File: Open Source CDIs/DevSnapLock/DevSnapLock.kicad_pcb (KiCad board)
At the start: 2 copper layers, 65.5 x 31.5 mm, 19 parts, among them J1 MAG, J2 COIL, J3 GtD, J4 AtG, J5 scrD, J6 lD, J7 aD, J8 aC, Q1 TIC106

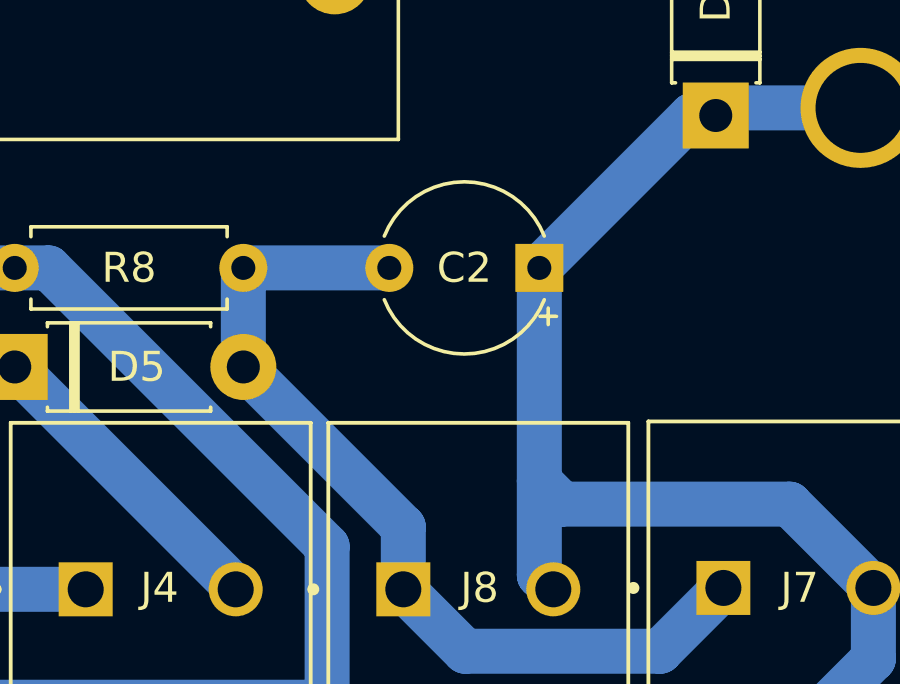
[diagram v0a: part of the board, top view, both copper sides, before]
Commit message: Added new CDIs and updated README
Added the DevPot_v2 CDI, updated the readme to include all of the new CDIs and included images for each. Also add production exports for all the boards.
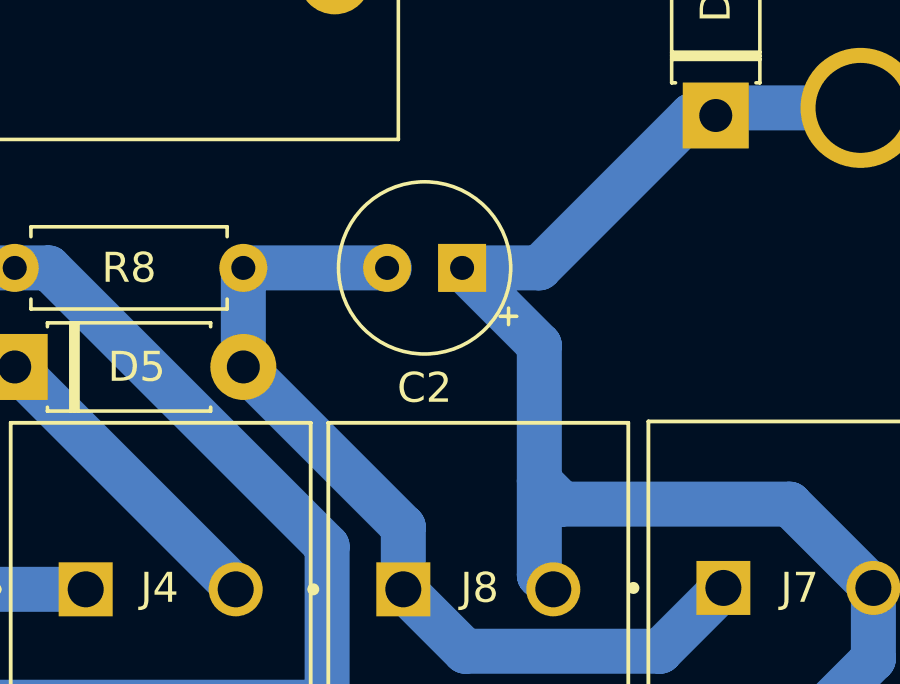
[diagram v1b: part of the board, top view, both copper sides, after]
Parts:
- C2: footprint Capacitor_THT:CP_Radial_Tantal_D5.5mm_P5.00mm -> Capacitor_THT:CP_Radial_Tantal_D5.5mm_P2.50mm
- moved C2 2.57 mm to (185.6, 107.2)
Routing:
- net GND: track 157.2 -> 160.8 mm
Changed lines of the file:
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@@
     (pad "2" thru_hole circle (at 2.5 0) (size 1.8 1.8) (drill 1.2) (layers "*.Cu" "*.Mask")
       (net 3 "GND") (pinfunction "Pin_2") (pintype "passive") (solder_mask_margin 0.102))
+    (model "${KIPRJMOD}/1792863.step"
+      (offset (xyz -5 -3 0))
+      (scale (xyz 1 1 1))
+      (rotate (xyz 0 0 0))
+    )
   )
   (footprint "Connector_Wire:SolderWire-2.5sqmm_1x02_P7.2mm_D2.4mm_OD3.6mm" (layer "F.Cu")
@@
     (pad "2" thru_hole circle (at 2.5 0) (size 1.8 1.8) (drill 1.2) (layers "*.Cu" "*.Mask")
       (net 3 "GND") (pinfunction "Pin_2") (pintype "passive") (solder_mask_margin 0.102))
+    (model "${KIPRJMOD}/1792863.step"
+      (offset (xyz -5 -3 0))
+      (scale (xyz 1 1 1))
+      (rotate (xyz 0 0 0))
+    )
   )
   (footprint "TE_1792863:TE_1792863" (layer "F.Cu")
@@
     (pad "2" thru_hole circle (at 2.5 0 180) (size 1.8 1.8) (drill 1.2) (layers "*.Cu" "*.Mask")
       (net 6 "Net-(D1-A)") (pinfunction "Pin_2") (pintype "passive") (solder_mask_margin 0.102))
-  )
-  (footprint "Capacitor_THT:CP_Radial_Tantal_D5.5mm_P5.00mm" (layer "F.Cu")
-    (at 188.174 107.188 180)
-    (descr "CP, Radial_Tantal series, Radial, pin pitch=5.00mm, , diameter=5.5mm, Tantal Electrolytic Capacitor, http://cdn-reichelt.de/documents/datenblatt/B300/TANTAL-TB-Serie%23.pdf")
-    (tags "CP Radial_Tantal series Radial pin pitch 5.00mm  diameter 5.5mm Tantal Electrolytic Capacitor")
+    (model "${KIPRJMOD}/1792863.step"
+      (offset (xyz 5 3 0))
+      (scale (xyz 1 1 1))
+      (rotate (xyz 0 0 -180))
+    )
+  )
+  (footprint "Capacitor_THT:CP_Radial_Tantal_D5.5mm_P2.50mm" (layer "F.Cu")
+    (at 185.600369 107.188 180)
+    (descr "CP, Radial_Tantal series, Radial, pin pitch=2.50mm, , diameter=5.5mm, Tantal Electrolytic Capacitor, http://cdn-reichelt.de/documents/datenblatt/B300/TANTAL-TB-Serie%23.pdf")
+    (tags "CP Radial_Tantal series Radial pin pitch 2.50mm  diameter 5.5mm Tantal Electrolytic Capacitor")
     (property "Sheetfile" "DevSnapLock.kicad_sch")
     (property "Sheetname" "")
@@
     (property "ki_keywords" "cap capacitor")
     (attr through_hole)
-    (fp_text reference "C2" (at 2.5 0) (layer "F.SilkS")
-        (effects (font (size 1 1) (thickness 0.15)))
-    )
-    (fp_text value "0.47u" (at 2.5 4) (layer "F.Fab")
-        (effects (font (size 1 1) (thickness 0.15)))
-    )
-    (fp_text user "${REFERENCE}" (at 2.5 0) (layer "F.Fab")
-        (effects (font (size 1 1) (thickness 0.15)))
-    )
-    (fp_line (start -0.572262 -1.615) (end -0.022262 -1.615)
-      (stroke (width 0.12) (type solid)) (layer "F.SilkS"))
-    (fp_line (start -0.297262 -1.89) (end -0.297262 -1.34)
-      (stroke (width 0.12) (type solid)) (layer "F.SilkS"))
-    (fp_arc (start -0.167077 -1.06) (mid 2.5 -2.87) (end 5.167077 -1.06)
-      (stroke (width 0.12) (type solid)) (layer "F.SilkS"))
-    (fp_arc (start 5.167077 1.06) (mid 2.5 2.87) (end -0.167077 1.06)
-      (stroke (width 0.12) (type solid)) (layer "F.SilkS"))
-    (fp_circle (center 2.5 0) (end 6.22 0)
+    (fp_text reference "C2" (at 1.25 -4 180) (layer "F.SilkS")
+        (effects (font (size 1 1) (thickness 0.15)))
+    )
+    (fp_text value "0.47u" (at 1.25 4 180) (layer "F.Fab")
+        (effects (font (size 1 1) (thickness 0.15)))
+    )
+    (fp_text user "${REFERENCE}" (at 1.25 0 180) (layer "F.Fab")
+        (effects (font (size 1 1) (thickness 0.15)))
+    )
+    (fp_line (start -1.822262 -1.615) (end -1.272262 -1.615)
+      (stroke (width 0.12) (type solid)) (layer "F.SilkS"))
+    (fp_line (start -1.547262 -1.89) (end -1.547262 -1.34)
+      (stroke (width 0.12) (type solid)) (layer "F.SilkS"))
+    (fp_circle (center 1.25 0) (end 4.12 0)
+      (stroke (width 0.12) (type solid)) (fill none) (layer "F.SilkS"))
+    (fp_circle (center 1.25 0) (end 4.25 0)
       (stroke (width 0.05) (type solid)) (fill none) (layer "F.CrtYd"))
-    (fp_line (start 0.150869 -1.1975) (end 0.700869 -1.1975)
-      (stroke (width 0.1) (type solid)) (layer "F.Fab"))
-    (fp_line (start 0.425869 -1.4725) (end 0.425869 -0.9225)
-      (stroke (width 0.1) (type solid)) (layer "F.Fab"))
-    (fp_circle (center 2.5 0) (end 5.25 0)
+    (fp_line (start -1.099131 -1.1975) (end -0.549131 -1.1975)
+      (stroke (width 0.1) (type solid)) (layer "F.Fab"))
+    (fp_line (start -0.824131 -1.4725) (end -0.824131 -0.9225)
+      (stroke (width 0.1) (type solid)) (layer "F.Fab"))
+    (fp_circle (center 1.25 0) (end 4 0)
       (stroke (width 0.1) (type solid)) (fill none) (layer "F.Fab"))
     (pad "1" thru_hole rect (at 0 0 180) (size 1.6 1.6) (drill 0.8) (layers "*.Cu" "*.Mask")
       (net 3 "GND") (pintype "passive"))
-    (pad "2" thru_hole circle (at 5 0 180) (size 1.6 1.6) (drill 0.8) (layers "*.Cu" "*.Mask")
+    (pad "2" thru_hole circle (at 2.5 0 180) (size 1.6 1.6) (drill 0.8) (layers "*.Cu" "*.Mask")
       (net 4 "Net-(D5-A)") (pintype "passive"))
-    (model "${KICAD6_3DMODEL_DIR}/Capacitor_THT.3dshapes/CP_Radial_Tantal_D5.5mm_P5.00mm.wrl"
+    (model "${KICAD6_3DMODEL_DIR}/Capacitor_THT.3dshapes/CP_Radial_Tantal_D5.5mm_P2.50mm.wrl"
       (offset (xyz 0 0 0))
       (scale (xyz 1 1 1))
@@
     (pad "2" thru_hole circle (at 2.5 0) (size 1.8 1.8) (drill 1.2) (layers "*.Cu" "*.Mask")
       (net 7 "Net-(D5-K)") (pinfunction "Pin_2") (pintype "passive") (solder_mask_margin 0.102))
+    (model "${KIPRJMOD}/1792863.step"
+      (offset (xyz -5 -3 0))
+      (scale (xyz 1 1 1))
+      (rotate (xyz 0 0 0))
+    )
   )
   (footprint "Resistor_THT:R_Axial_DIN0207_L6.3mm_D2.5mm_P7.62mm_Horizontal" (layer "F.Cu")
@@
     (pad "2" thru_hole circle (at 2.5 0) (size 1.8 1.8) (drill 1.2) (layers "*.Cu" "*.Mask")
       (net 9 "Net-(J3-Pin_2)") (pinfunction "Pin_2") (pintype "passive") (solder_mask_margin 0.102))
+    (model "${KIPRJMOD}/1792863.step"
+      (offset (xyz -5 -3 0))
+      (scale (xyz 1 1 1))
+      (rotate (xyz 0 0 0))
+    )
   )
   (footprint "Diode_THT:D_DO-41_SOD81_P7.62mm_Horizontal" (layer "F.Cu")
@@
     (pad "2" thru_hole circle (at 2.5 0) (size 1.8 1.8) (drill 1.2) (layers "*.Cu" "*.Mask")
       (net 3 "GND") (pinfunction "Pin_2") (pintype "passive") (solder_mask_margin 0.102))
+    (model "${KIPRJMOD}/1792863.step"
+      (offset (xyz -5 -3 0))
+      (scale (xyz 1 1 1))
+      (rotate (xyz 0 0 0))
+    )
   )
   (footprint "Package_TO_SOT_THT:TO-220-3_Vertical" (layer "F.Cu")
@@
   (segment (start 188.936 115.062) (end 188.174 114.3) (width 1.5) (layer "B.Cu") (net 3))
   (segment (start 181.864 122.428) (end 197.104 122.428) (width 1.5) (layer "B.Cu") (net 3))
-  (segment (start 194.056 102.108) (end 193.254 102.108) (width 1.5) (layer "B.Cu") (net 3))
   (segment (start 144.12 119.706) (end 139.12 119.706) (width 1.5) (layer "B.Cu") (net 3))
-  (segment (start 188.174 107.188) (end 188.174 114.3) (width 1.5) (layer "B.Cu") (net 3))
+  (segment (start 185.600369 107.188) (end 188.174 109.761631) (width 1.5) (layer "B.Cu") (net 3))
+  (segment (start 193.254 102.108) (end 188.174 107.188) (width 1.5) (layer "B.Cu") (net 3))
   (segment (start 196.516 115.062) (end 188.936 115.062) (width 1.5) (layer "B.Cu") (net 3))
   (segment (start 197.104 122.428) (end 199.31 120.222) (width 1.5) (layer "B.Cu") (net 3))
@@
   (segment (start 170.688 107.188) (end 171.81937 107.188) (width 1.5) (layer "B.Cu") (net 3))
   (segment (start 181.102 121.666) (end 181.864 122.428) (width 1.5) (layer "B.Cu") (net 3))
+  (segment (start 188.174 109.761631) (end 188.174 114.3) (width 1.5) (layer "B.Cu") (net 3))
+  (segment (start 194.056 102.108) (end 193.254 102.108) (width 1.5) (layer "B.Cu") (net 3))
   (segment (start 188.174 114.3) (end 188.174 117.4355) (width 1.5) (layer "B.Cu") (net 3))
   (segment (start 170.688 107.188) (end 160.528 107.188) (width 1.5) (layer "B.Cu") (net 3))
   (segment (start 140.462 106.934) (end 140.462 103.422) (width 1.5) (layer "B.Cu") (net 3))
   (segment (start 142.24 106.934) (end 140.462 106.934) (width 1.5) (layer "B.Cu") (net 3))
-  (segment (start 193.254 102.108) (end 188.174 107.188) (width 1.5) (layer "B.Cu") (net 3))
+  (segment (start 188.174 107.188) (end 185.600369 107.188) (width 1.5) (layer "B.Cu") (net 3))
   (segment (start 142.512 107.206) (end 142.24 106.934) (width 1.5) (layer "B.Cu") (net 3))
   (segment (start 142.512 111.742) (end 142.512 107.206) (width 1.5) (layer "B.Cu") (net 3))
